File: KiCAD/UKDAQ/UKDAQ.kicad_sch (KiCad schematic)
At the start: 8 parts

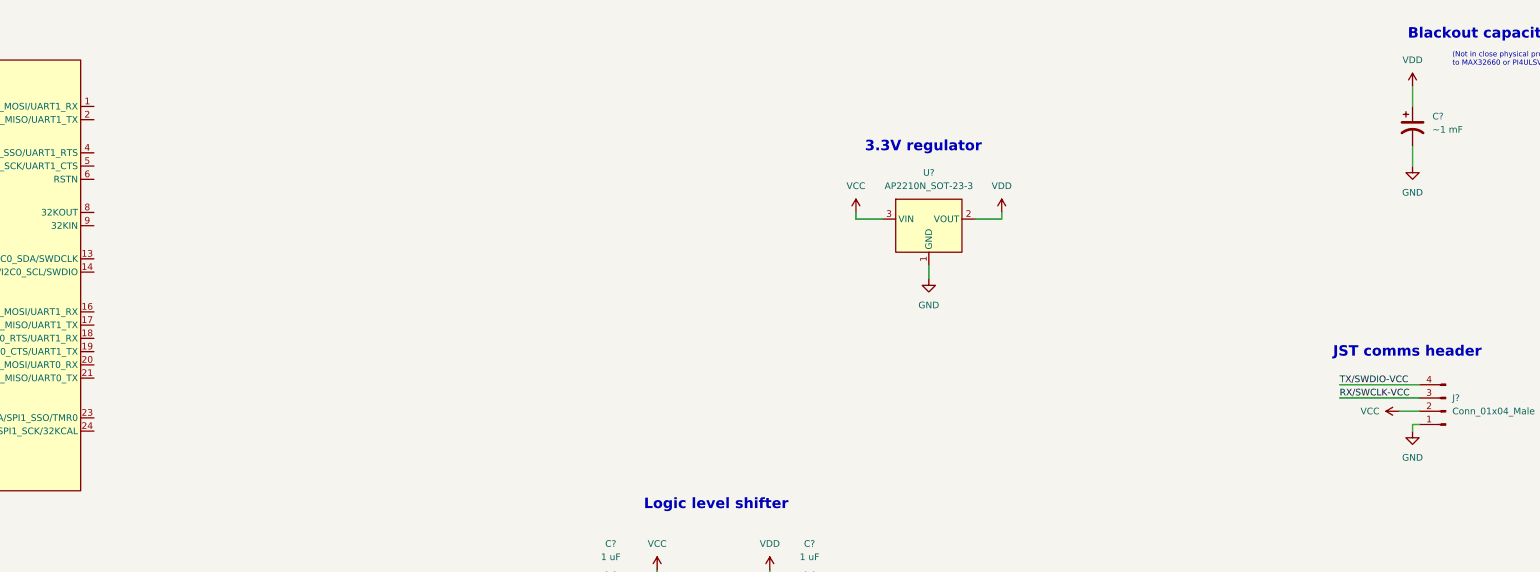
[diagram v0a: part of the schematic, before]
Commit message: 5 pin header for reset pin instead of 4
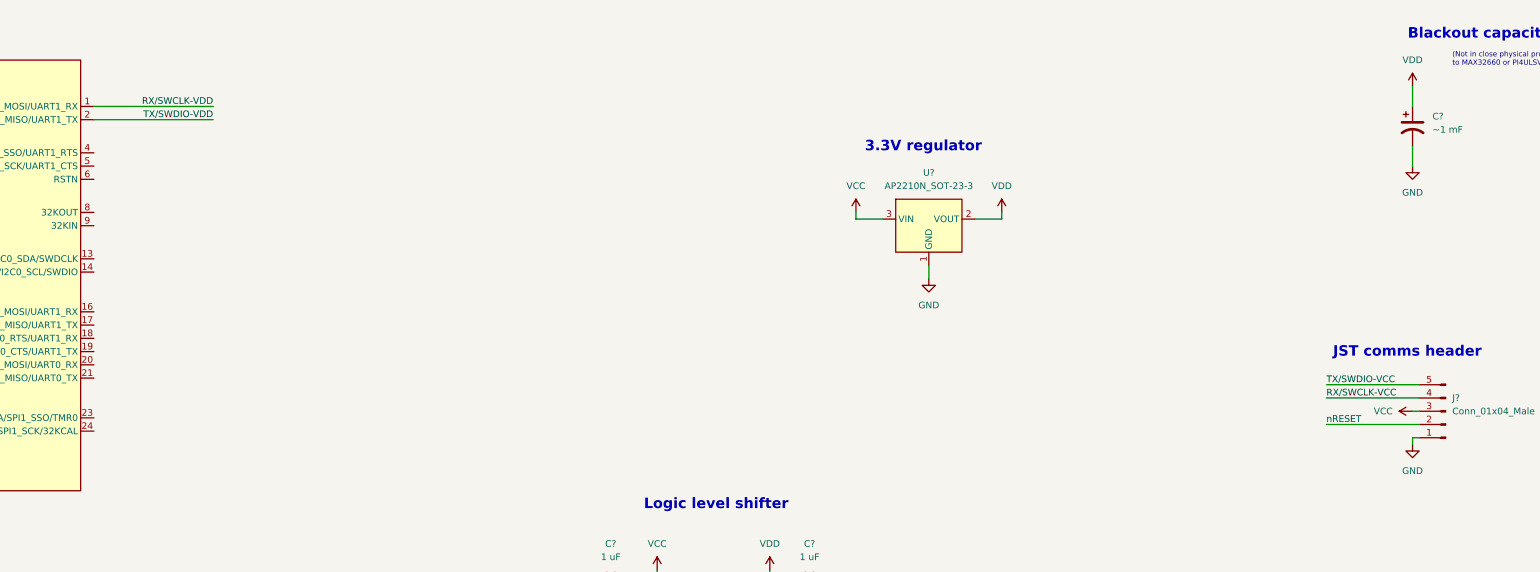
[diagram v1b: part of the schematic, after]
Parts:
- J?: symbol Connector:Conn_01x04_Male -> Connector:Conn_01x05_Male
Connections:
- net RX/SWCLK-VCC: now also J?.4 (Pin_4); no longer J?.3 (Pin_3)
- net RX/SWCLK-VDD: now also U?.1 (P0.1/SWDCLK/SPI1_MOSI/UART1_RX)
- net TX/SWDIO-VCC: now also J?.5 (Pin_5); no longer J?.4 (Pin_4)
- net TX/SWDIO-VDD: now also U?.2 (P0.0/SWDIO/SPI1_MISO/UART1_TX)
- net VCC: now also J?.3 (Pin_3); no longer J?.2 (Pin_2)
- new net nRESET: J?.2 (Pin_2)
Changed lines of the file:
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@@
     (stroke (width 0) (type default) (color 0 0 0 0))
   )
-  (wire (pts (xy 361.95 201.93) (xy 360.68 201.93))
-    (stroke (width 0) (type default) (color 0 0 0 0))
-  )
-  (wire (pts (xy 346.71 194.31) (xy 361.95 194.31))
+  (wire (pts (xy 344.17 194.31) (xy 361.95 194.31))
     (stroke (width 0) (type default) (color 0 0 0 0))
   )
@@
     (stroke (width 0) (type default) (color 0 0 0 0))
   )
-  (wire (pts (xy 358.14 199.39) (xy 361.95 199.39))
-    (stroke (width 0) (type default) (color 0 0 0 0))
-  )
   (wire (pts (xy 81.28 127) (xy 78.74 127))
     (stroke (width 0) (type default) (color 0 0 0 0))
   )
+  (wire (pts (xy 361.95 204.47) (xy 360.68 204.47))
+    (stroke (width 0) (type default) (color 0 0 0 0))
+  )
   (wire (pts (xy 237.49 229.87) (xy 237.49 232.41))
     (stroke (width 0) (type default) (color 0 0 0 0))
@@
     (stroke (width 0) (type default) (color 0 0 0 0))
   )
+  (wire (pts (xy 344.17 201.93) (xy 361.95 201.93))
+    (stroke (width 0) (type default) (color 0 0 0 0))
+  )
   (wire (pts (xy 76.2 217.17) (xy 76.2 218.44))
     (stroke (width 0) (type default) (color 0 0 0 0))
@@
     (stroke (width 0) (type default) (color 0 0 0 0))
   )
+  (wire (pts (xy 107.95 140.97) (xy 130.81 140.97))
+    (stroke (width 0) (type default) (color 0 0 0 0))
+  )
   (wire (pts (xy 234.95 252.73) (xy 237.49 252.73))
     (stroke (width 0) (type default) (color 0 0 0 0))
@@
     (stroke (width 0) (type default) (color 0 0 0 0))
   )
-  (wire (pts (xy 346.71 196.85) (xy 361.95 196.85))
+  (wire (pts (xy 344.17 196.85) (xy 361.95 196.85))
+    (stroke (width 0) (type default) (color 0 0 0 0))
+  )
+  (wire (pts (xy 360.68 204.47) (xy 360.68 205.74))
     (stroke (width 0) (type default) (color 0 0 0 0))
   )
@@
     (stroke (width 0) (type default) (color 0 0 0 0))
   )
+  (wire (pts (xy 360.68 199.39) (xy 361.95 199.39))
+    (stroke (width 0) (type default) (color 0 0 0 0))
+  )
   (wire (pts (xy 200.66 232.41) (xy 200.66 234.95))
     (stroke (width 0) (type default) (color 0 0 0 0))
@@
     (stroke (width 0) (type default) (color 0 0 0 0))
   )
-  (wire (pts (xy 360.68 201.93) (xy 360.68 203.2))
+  (wire (pts (xy 107.95 143.51) (xy 130.81 143.51))
     (stroke (width 0) (type default) (color 0 0 0 0))
   )
@@
     (effects (font (size 2 2) bold) (justify right bottom))
   )
+  (label "nRESET" (at 344.17 201.93 0)
+    (effects (font (size 1.27 1.27)) (justify left bottom))
+  )
   (label "RX{slash}SWCLK-VCC" (at 200.66 248.92 0)
     (effects (font (size 1.27 1.27)) (justify left bottom))
   )
-  (label "RX{slash}SWCLK-VCC" (at 346.71 196.85 0)
+  (label "RX{slash}SWCLK-VCC" (at 344.17 196.85 0)
     (effects (font (size 1.27 1.27)) (justify left bottom))
   )
-  (label "TX{slash}SWDIO-VCC" (at 346.71 194.31 0)
+  (label "TX{slash}SWDIO-VCC" (at 344.17 194.31 0)
     (effects (font (size 1.27 1.27)) (justify left bottom))
   )
@@
     (effects (font (size 1.27 1.27)) (justify left bottom))
   )
+  (label "RX{slash}SWCLK-VDD" (at 130.81 140.97 180)
+    (effects (font (size 1.27 1.27)) (justify right bottom))
+  )
   (label "RX{slash}SWCLK-VDD" (at 251.46 248.92 180)
+    (effects (font (size 1.27 1.27)) (justify right bottom))
+  )
+  (label "TX{slash}SWDIO-VDD" (at 130.81 143.51 180)
     (effects (font (size 1.27 1.27)) (justify right bottom))
   )
@@
     (pin "2")
   )
-  (symbol (lib_id "power:GND") (at 360.68 203.2 0) (unit 1)
-    (in_bom yes) (on_board yes) (fields_autoplaced)
-    (property "Reference" "#PWR?" (id 0) (at 360.68 209.55 0)
-      (effects (font (size 1.27 1.27)) hide)
-    )
-    (property "Value" "GND" (id 1) (at 360.68 208.28 0))
-    (property "Footprint" "" (id 2) (at 360.68 203.2 0)
-      (effects (font (size 1.27 1.27)) hide)
-    )
-    (property "Datasheet" "" (id 3) (at 360.68 203.2 0)
+  (symbol (lib_id "power:GND") (at 360.68 205.74 0) (unit 1)
+    (in_bom yes) (on_board yes) (fields_autoplaced)
+    (property "Reference" "#PWR?" (id 0) (at 360.68 212.09 0)
+      (effects (font (size 1.27 1.27)) hide)
+    )
+    (property "Value" "GND" (id 1) (at 360.68 210.82 0))
+    (property "Footprint" "" (id 2) (at 360.68 205.74 0)
+      (effects (font (size 1.27 1.27)) hide)
+    )
+    (property "Datasheet" "" (id 3) (at 360.68 205.74 0)
       (effects (font (size 1.27 1.27)) hide)
     )
@@
     (pin "3")
   )
-  (symbol (lib_id "Connector:Conn_01x04_Male") (at 367.03 199.39 180) (unit 1)
+  (symbol (lib_id "Connector:Conn_01x05_Male") (at 367.03 199.39 180) (unit 1)
     (in_bom yes) (on_board yes) (fields_autoplaced)
     (property "Reference" "J?" (id 0) (at 368.3 196.8499 0)
@@
     (pin "3")
     (pin "4")
+    (pin "5")
   )
   (symbol (lib_id "power:VDD") (at 237.49 229.87 0) (unit 1)
@@
     (pin "1")
   )
-  (symbol (lib_id "power:VCC") (at 358.14 199.39 90) (unit 1)
-    (in_bom yes) (on_board yes) (fields_autoplaced)
-    (property "Reference" "#PWR?" (id 0) (at 361.95 199.39 0)
-      (effects (font (size 1.27 1.27)) hide)
-    )
-    (property "Value" "VCC" (id 1) (at 354.33 199.3899 90)
+  (symbol (lib_id "power:VCC") (at 360.68 199.39 90) (unit 1)
+    (in_bom yes) (on_board yes) (fields_autoplaced)
+    (property "Reference" "#PWR?" (id 0) (at 364.49 199.39 0)
+      (effects (font (size 1.27 1.27)) hide)
+    )
+    (property "Value" "VCC" (id 1) (at 356.87 199.3899 90)
       (effects (font (size 1.27 1.27)) (justify left))
     )
-    (property "Footprint" "" (id 2) (at 358.14 199.39 0)
-      (effects (font (size 1.27 1.27)) hide)
-    )
-    (property "Datasheet" "" (id 3) (at 358.14 199.39 0)
-      (effects (font (size 1.27 1.27)) hide)
-    )
+    (property "Footprint" "" (id 2) (at 360.68 199.39 0)
+      (effects (font (size 1.27 1.27)) hide)
+    )
+    (property "Datasheet" "" (id 3) (at 360.68 199.39 0)
+      (effects (font (size 1.27 1.27)) hide)
+    )

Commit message: some more updates before bedtime
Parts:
- added C? (x2): 6 pF, symbol Device:C
- added C?: 100 nF, symbol Device:C
- added R?: 10k, symbol Device:R
- added R?: 10, symbol Device:R
- added Y?: Crystal, symbol Device:Crystal
- J?: value Conn_01x04_Male -> 5 pin Molex (0537800570)
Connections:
- net GND: now also C?.2, C?.2, R?.2
- net VDD: now also R?.1
- net nRESET: now also U?.6 (RSTN), C?.1, R?.2
- net at U?.8 (32KOUT): now also C?.1, Y?.2
- net at U?.9 (32KIN): now also C?.1, Y?.1
- new net: C?.2, R?.1
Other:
- note added: "External comms header"
- note removed: "JST comms header"

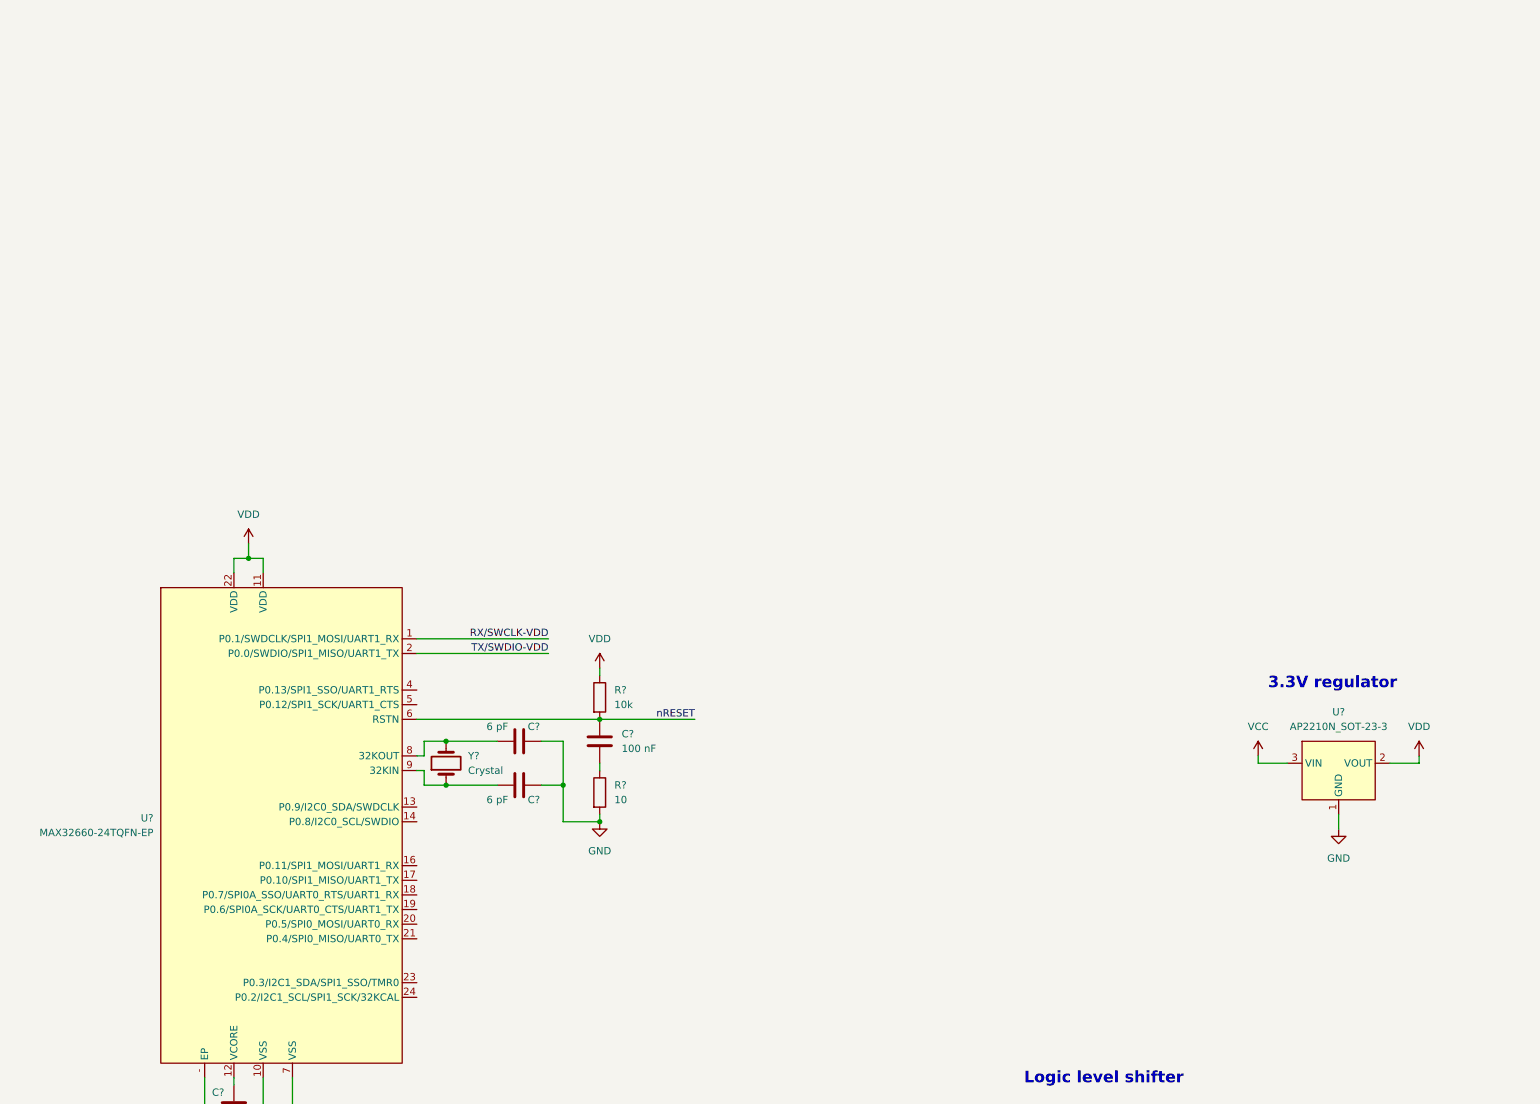
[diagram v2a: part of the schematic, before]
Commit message: added bme280, swapped back to i2c because bno doesnt support spi, and finished max32660 subschematic
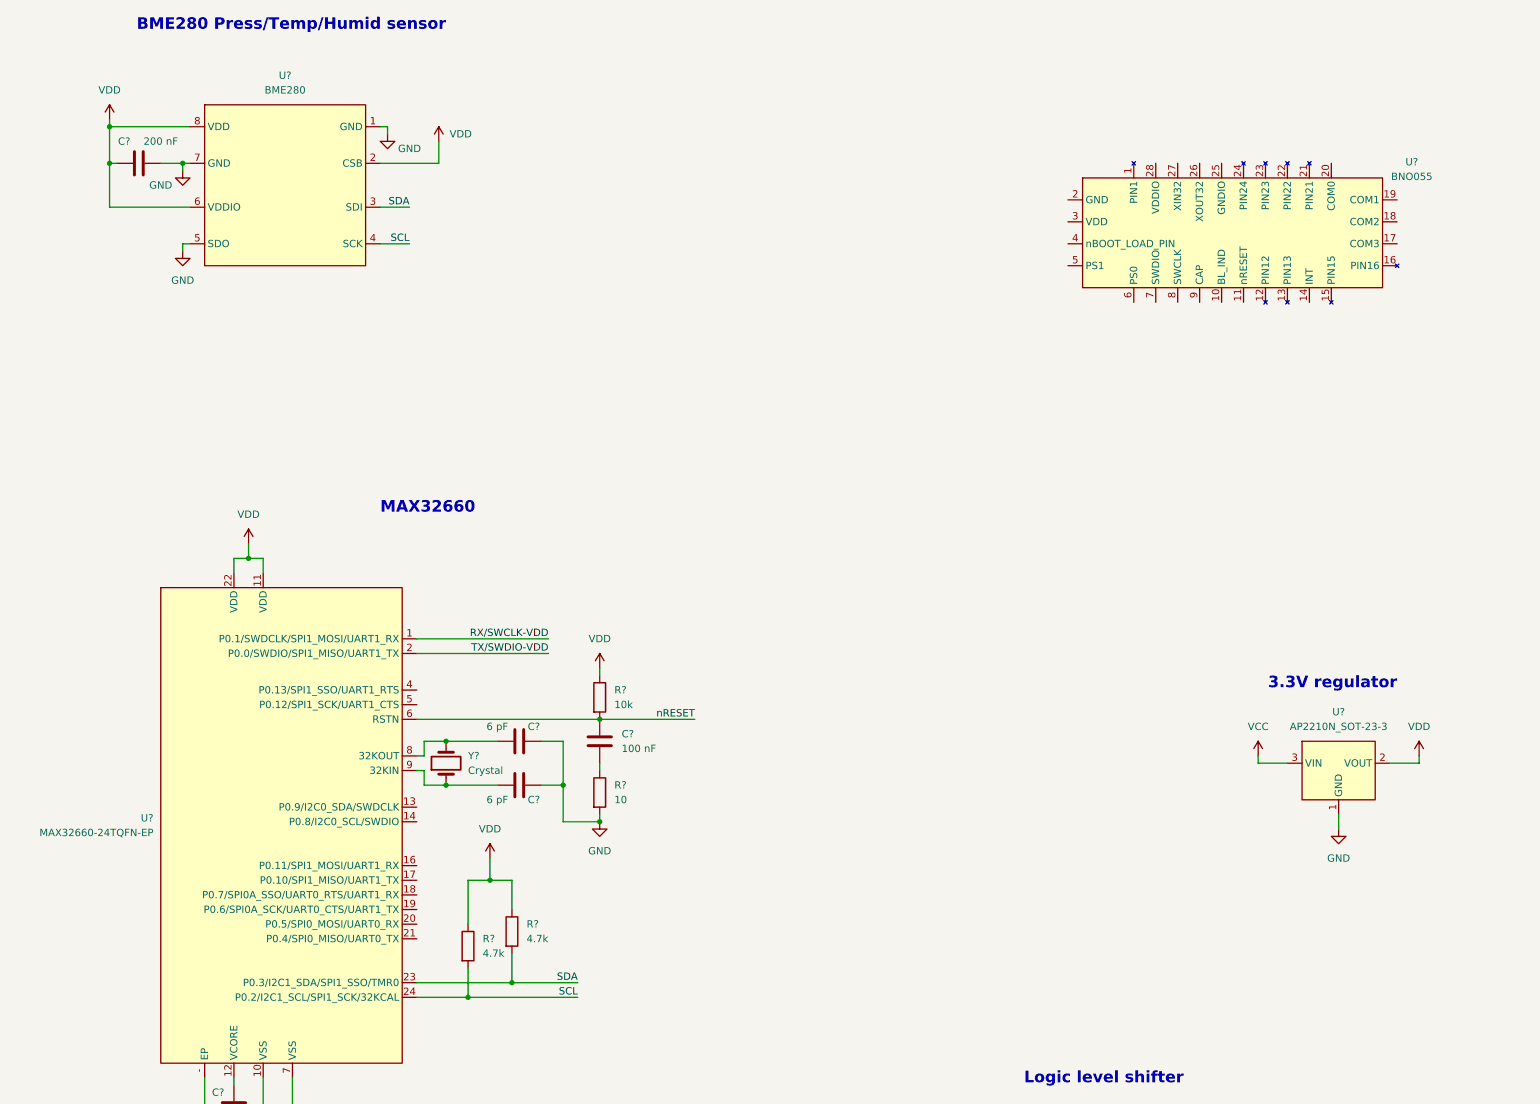
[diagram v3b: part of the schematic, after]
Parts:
- added C?: 200 nF, symbol Device:C
- added R? (x2): 4.7k, symbol Device:R
- added U?: BNO055, symbol Joseph:BNO055
- added U?: BME280, symbol Joseph:BME280
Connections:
- net GND: now also C?.2, U?.1 (GND), U?.5 (SDO), U?.7 (GND)
- net VDD: now also C?.1, R?.1, R?.1, U?.2 (CSB), U?.6 (VDDIO), U?.8 (VDD)
- net SDA: now reaches U?.23 (P0.3/I2C1_SDA/SPI1_SSO/TMR0)
- net SDA: now also R?.2, U?.3 (SDI)
- net SCL: now reaches U?.24 (P0.2/I2C1_SCL/SPI1_SCK/32KCAL)
- net SCL: now also R?.2, U?.4 (SCK)
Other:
- note added: "BME280 Press/Temp/Humid sensor"

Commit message: First version of schematic done! about to do design rule checks!
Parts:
- added C?: 120 nF, symbol Device:C
- added C?: 1 uF, symbol Device:C
- added R? (x2): 10k, symbol Device:R
- C?: value 200 nF -> 100 nF
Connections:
- net GND: now also U?.17 (COM3), U?.18 (COM2), U?.2 (GND), U?.25 (GNDIO), U?.5 (PS1), U?.6 (PS0), C?.1, C?.2
- net SCL: now also U?.19 (COM1)
- net SDA: now also U?.20 (COM0)
- net VDD: now also U?.28 (VDDIO), U?.3 (VDD), C?.1, R?.1, R?.1
- net nRESET: now also U?.11 (nRESET), R?.2
- net BNO_INTERRUPT: now reaches U?.14 (INT)
- net BNO_INTERRUPT: now also U?.16 (P0.11/SPI1_MOSI/UART1_RX)
- net at U?.4 (nBOOT_LOAD_PIN): now also R?.2
- net at U?.9 (CAP): now also C?.2
- no-connect marks 0 -> 14
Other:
- note added: "BNO055 9DOF IMU"
- note added: "MAX32660 microcontroller"
- moved on the sheet: C?, J?, R?, U?, Y?
